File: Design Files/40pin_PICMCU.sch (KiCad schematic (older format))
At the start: 29 parts, among them CON1 USB-MICRO-B, P1 CONN_10, P10 CONN_01X01, P2 CONN_10, P3 CONN_10, P4 CONN_10, P5 CONN_01X01, P6 ICSP, P7 CONN_01X01, P8 CONN_01X01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

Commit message: Changes Done
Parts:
- C1, C2, C3, C4, C5, C6: footprint (none) -> Capacitors_SMD:C_0603_HandSoldering; symbol C -> C-RESCUE-40pin_PICMCU
- CON1: footprint (none) -> Explore:USB_Micro-B_SMD_NEW_1
- D1, D3: footprint ~ -> Explore:LED-0603_NEW; symbol LED -> LED-RESCUE-40pin_PICMCU
- JP1: footprint (none) -> Pin_Headers:Pin_Header_Straight_1x02_Pitch2.54mm
- P1, P2, P3, P4: footprint (none) -> Pin_Headers:Pin_Header_Straight_1x10_Pitch2.54mm
- P10, P5, P8, P9: footprint (none) -> Connect:1pin
- P6: footprint (none) -> Pin_Headers:Pin_Header_Straight_1x06_Pitch2.54mm
- P7: footprint (none) -> E_Logo:Logo_8
- R1, R4, R5: footprint (none) -> Resistors_SMD:R_0603_HandSoldering; symbol R -> R-RESCUE-40pin_PICMCU
- R2, R3: footprint ~ -> Resistors_SMD:R_0603_HandSoldering; symbol R -> R-RESCUE-40pin_PICMCU
- SW1: footprint (none) -> Explore:SW_PUSH_SMALL_2pin_3D_xl_v1
- U***1: footprint (none) -> Housings_QFP:LQFP-44_10x10mm_Pitch0.8mm
- U1: footprint (none) -> Explore:cp2102_xl2
- X1: footprint (none) -> Crystals:Crystal_HC18-U_Vertical

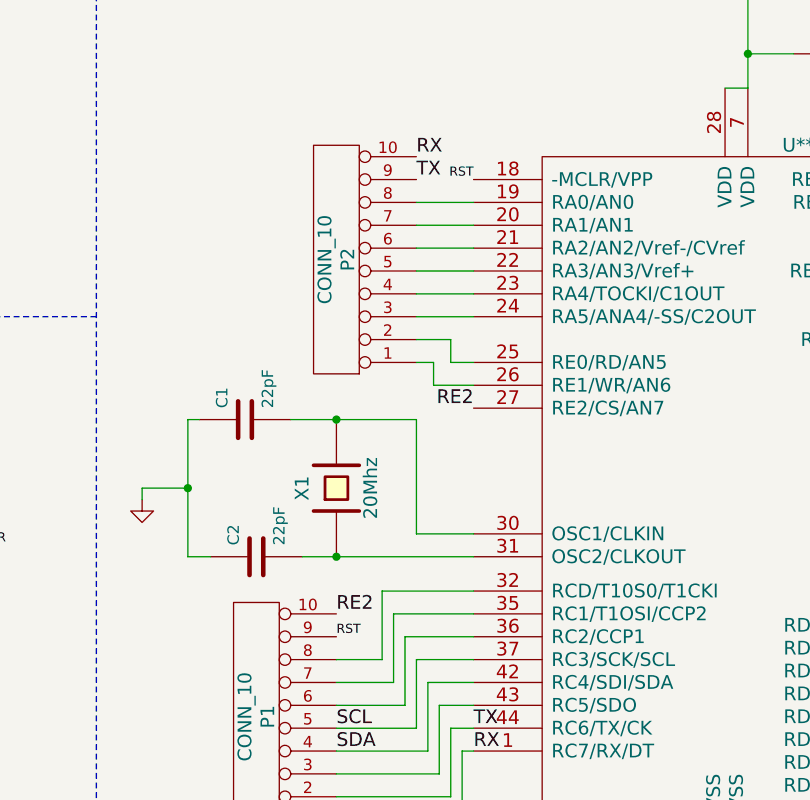
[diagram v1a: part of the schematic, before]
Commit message: Added Reset connectin
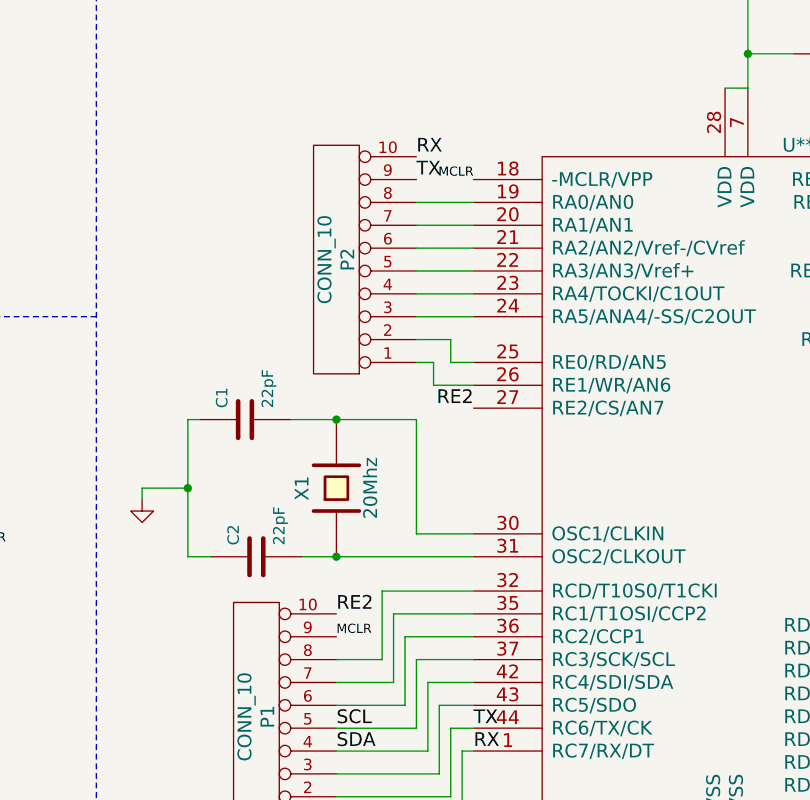
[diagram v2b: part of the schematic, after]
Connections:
- net RST is gone; now on net MCLR: P1.9 (P9), U***1.18 (-MCLR/VPP)
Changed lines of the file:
@@
 	1    0    0    1
 $EndComp
-Text Label 1650 3200 0    40   ~ 0
-MCLR
 Text Label 1350 2650 0    60   ~ 0
 +5V
@@
 Text Label 3250 3500 0    60   ~ 0
 RE2
-Text Label 3850 1600 2    40   ~ 0
-RST
-Text Label 3250 3600 0    40   ~ 0
-RST
 $Comp
 L CONN_10 P4
@@
 Wire Wire Line
 	4900 6250 5000 6250
+Text Label 1650 3200 0    40   ~ 0
+MCLR
+Text Label 3250 3600 0    40   ~ 0
+MCLR
+Text Label 3850 1600 2    40   ~ 0
+MCLR
 $EndSCHEMATC
